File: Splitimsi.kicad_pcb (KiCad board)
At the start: 2 copper layers, 118.2 x 100.1 mm, 33 parts, among them SW1 MX_RGB, SW10 MX_RGB, SW11 MX_RGB, SW12 MX_RGB, SW13 MX_RGB, SW14 MX_RGB, SW15 MX_RGB, SW16 MX_RGB, SW17 MX_RGB, SW18 MX_RGB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

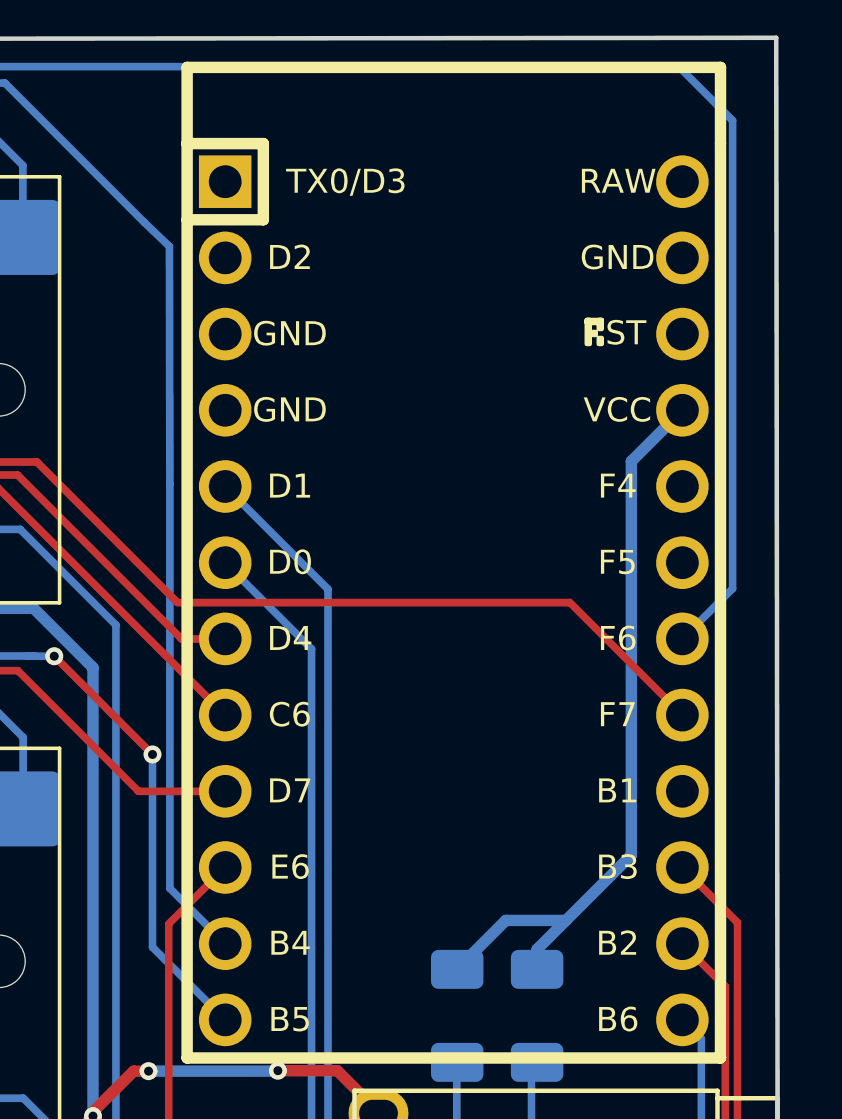
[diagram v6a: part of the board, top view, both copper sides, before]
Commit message: Front silkscreen creator and version info added
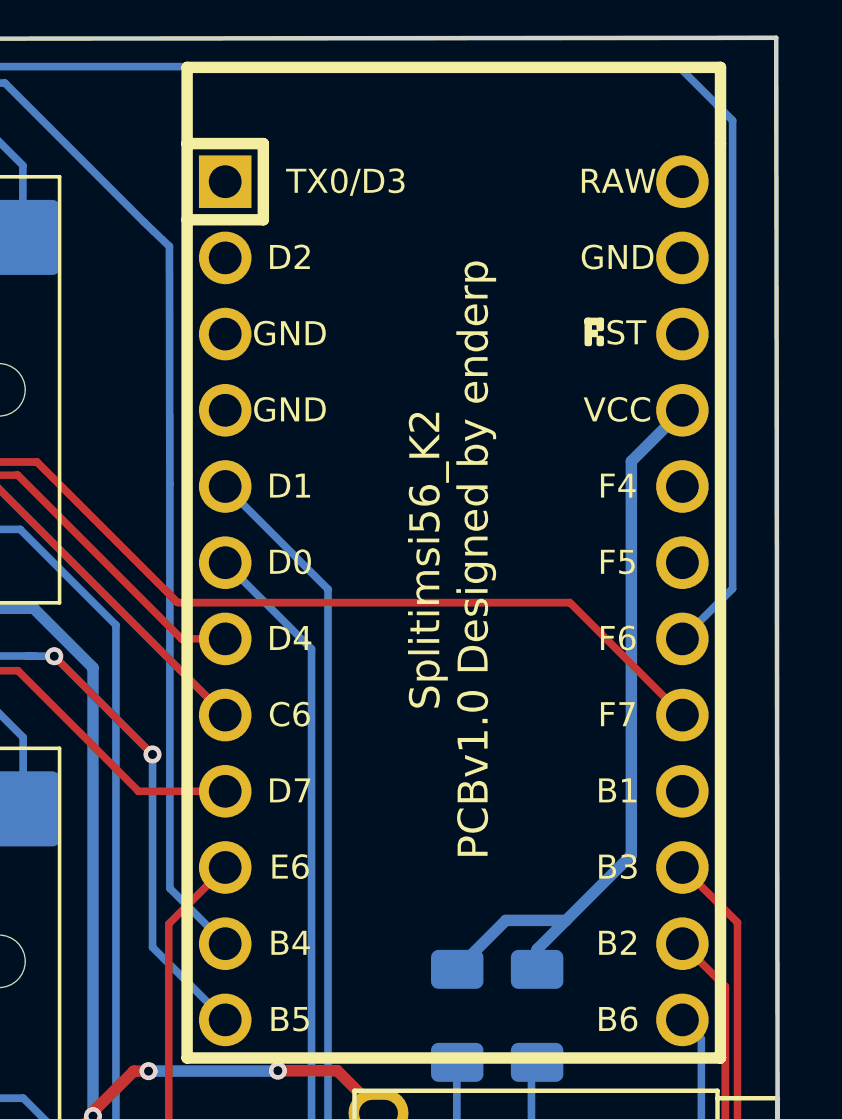
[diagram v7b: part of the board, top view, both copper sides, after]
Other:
- board text added: "Splitimsi56_K2 PCBv1.0 Designed by enderp"
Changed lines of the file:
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@@
     (property "Sheetname" "")
     (attr through_hole)
-    (fp_text reference "U2" (at 0 14.2 -90) (layer "Dwgs.User")
+    (fp_text reference "U2" (at 0.034304 4.602522 -90) (layer "Dwgs.User")
       (effects (font (size 1 1) (thickness 0.15)))
     )
@@
   (gr_line (start 20.32 97.79) (end 20.193 16.967909) (layer "Edge.Cuts") (width 0.15))
   (gr_line (start 20.32 116.967) (end 20.32 97.79) (layer "Edge.Cuts") (width 0.15))
+  (gr_text "Splitimsi56_K2\nPCBv1.0 Designed by enderp" (at 127.413902 34.230795 90) (layer "F.SilkS")
+    (effects (font (size 1 1) (thickness 0.2)))
+  )
   (segment (start 117.162291 56.424596) (end 117.145481 56.441406) (width 0.254) (layer "F.Cu") (net 1))
   (segment (start 117.145481 56.441406) (end 115.53879 56.441406) (width 0.254) (layer "F.Cu") (net 1))

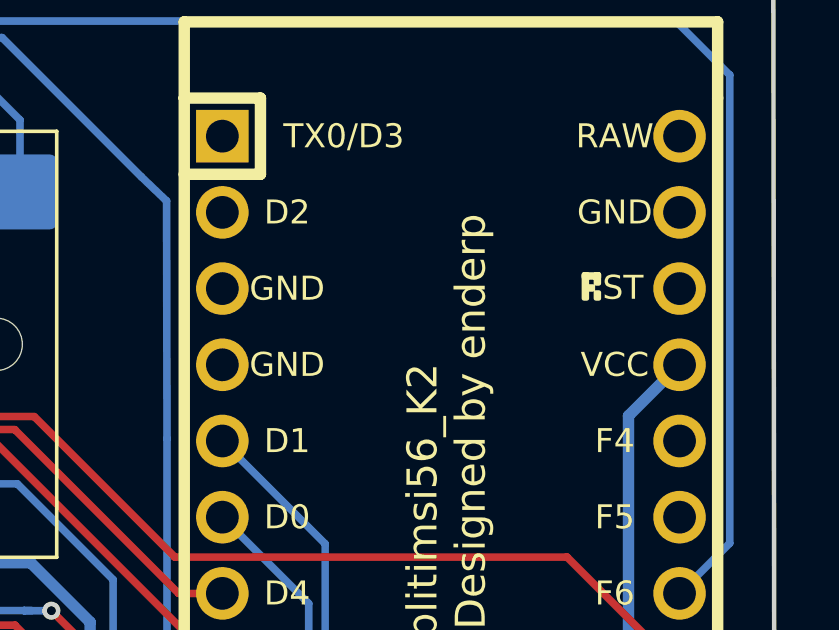
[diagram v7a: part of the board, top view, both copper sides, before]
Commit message: Reset button footprint placed
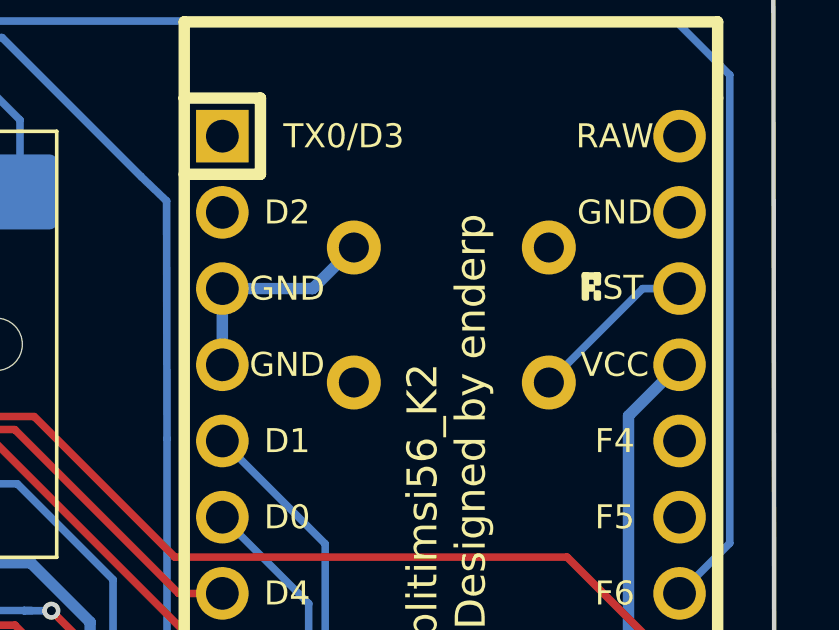
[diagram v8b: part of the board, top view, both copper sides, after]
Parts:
- added S1: TactSW_6x6_THT, aio3-misc:PushButton_6x6mm_TH_Pretty, B.Cu at (127.6, 27.6)
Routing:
- net GND: track 0.00 -> 7.49 mm
- net Net-(S1-Pad2)_1: track 0.00 -> 5.65 mm
